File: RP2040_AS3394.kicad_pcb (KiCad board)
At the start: 4 copper layers, 51.8 x 68.3 mm, 125 parts, among them J1 Conn_01x03, J2 TYPE-C-31-M-12, J3 Conn_01x05, J4 Conn_01x09, U1 RP2040, U2 NCP1117-3.3_SOT223, U3 W25Q128JVS, U4 LM324, U5 AS3394, U6 LM324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

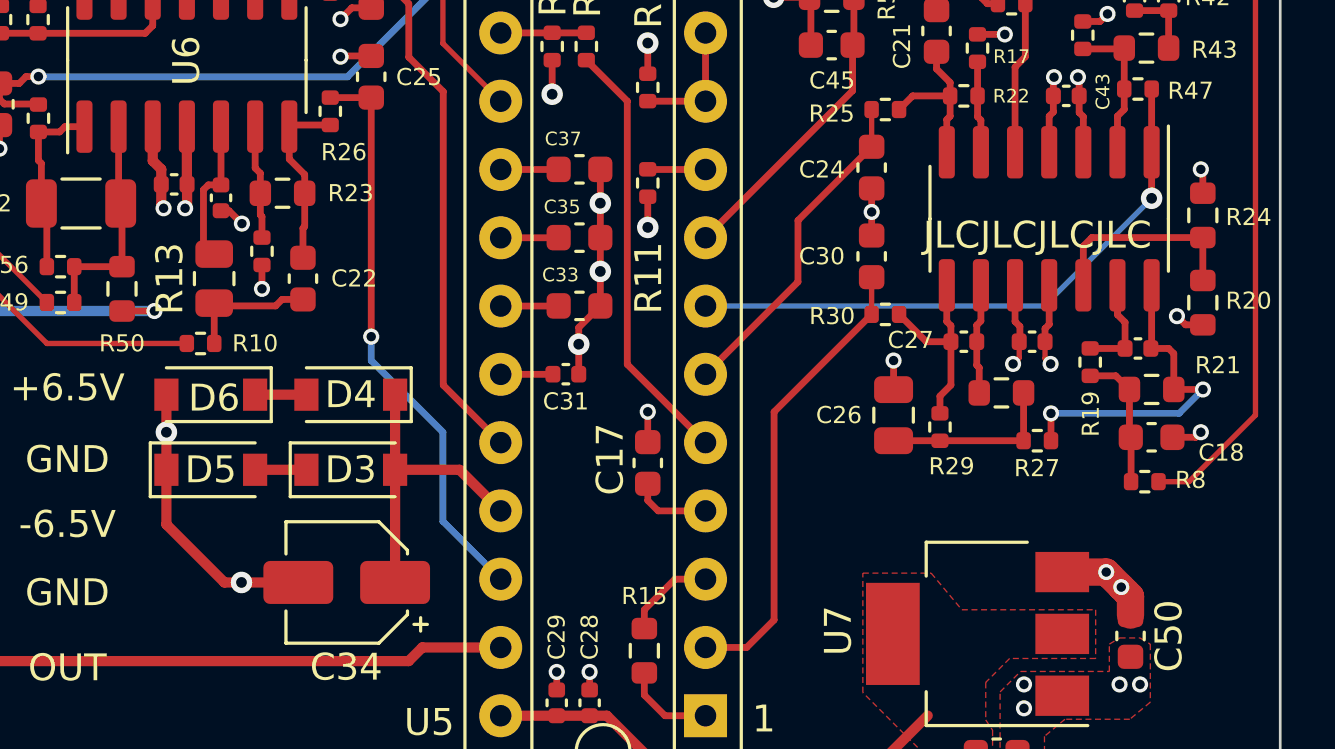
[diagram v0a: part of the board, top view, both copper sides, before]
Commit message: Updated to Kicad 7
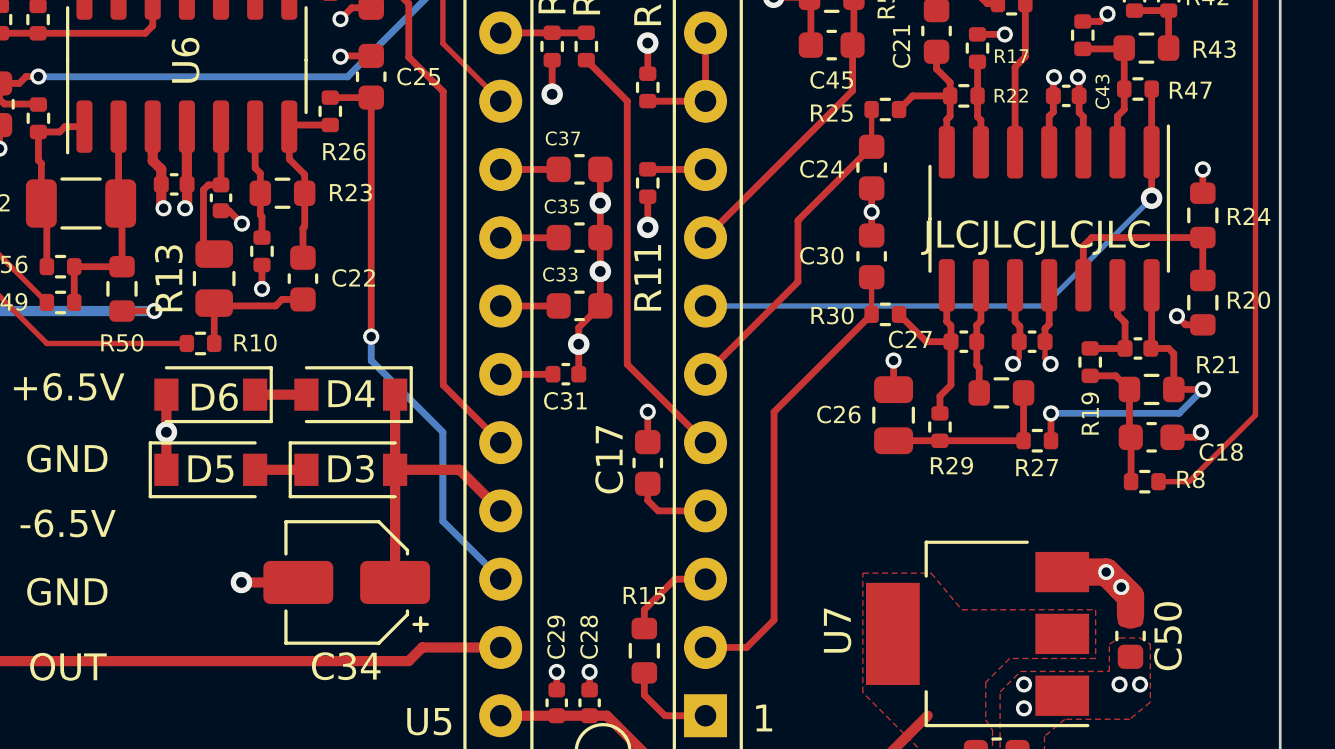
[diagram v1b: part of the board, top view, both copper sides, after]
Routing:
- net GND: track 95.2 -> 89.5 mm

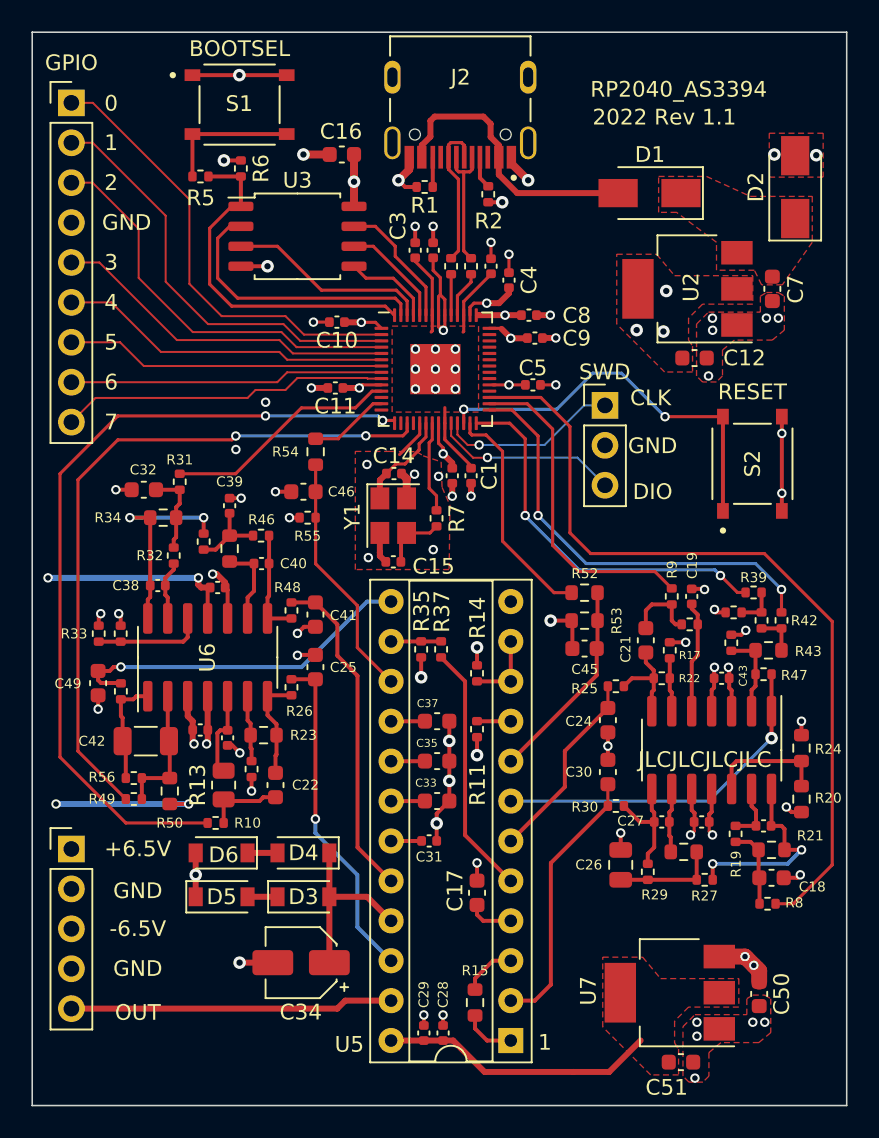
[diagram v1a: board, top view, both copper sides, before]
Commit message: Reworked op-amp bias to use 5V LDO reference instead of 6.5V vin
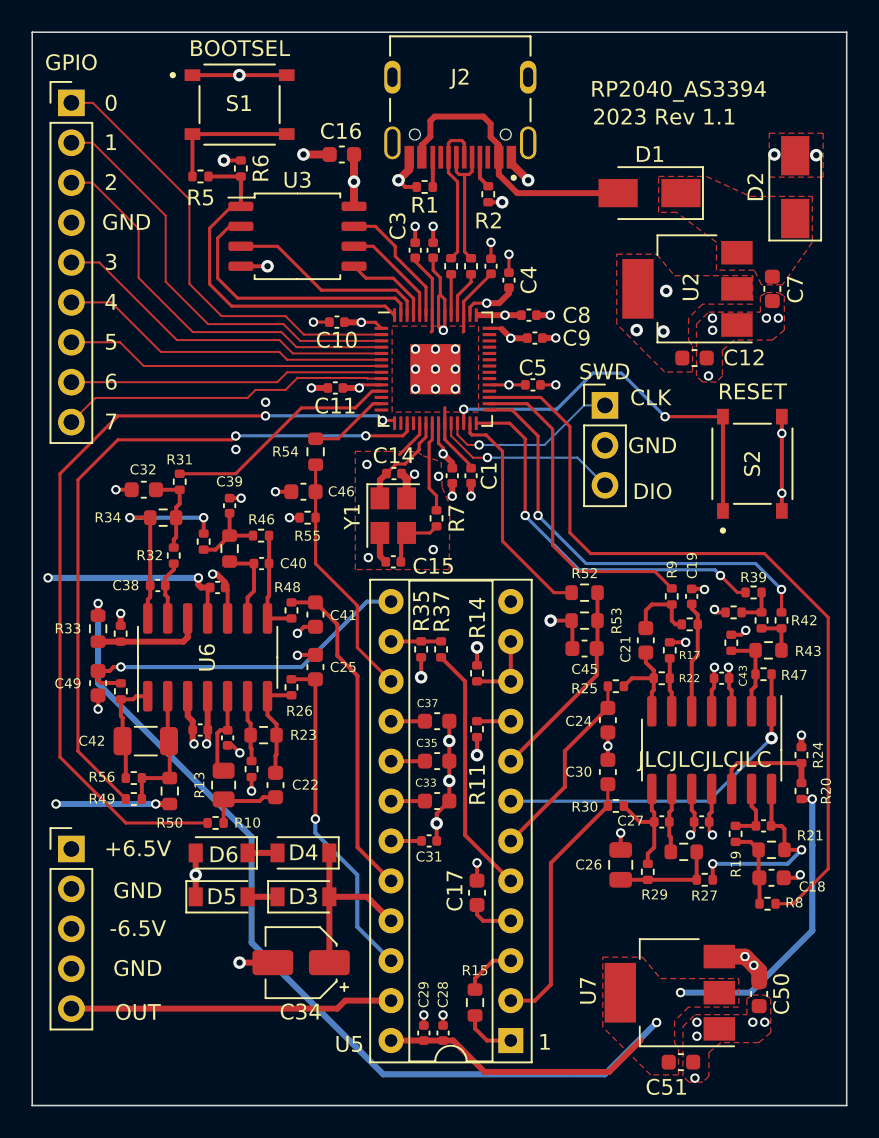
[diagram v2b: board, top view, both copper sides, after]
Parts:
- R20: value 3k -> 3k9; footprint Resistor_SMD:R_0603_1608Metric -> Resistor_SMD:R_0402_1005Metric
- R24: value 560 -> 1k; footprint Resistor_SMD:R_0603_1608Metric -> Resistor_SMD:R_0402_1005Metric
- R33: value 1k6 -> 6k2; footprint Resistor_SMD:R_0402_1005Metric -> Resistor_SMD:R_0603_1608Metric
- R36: value 300 -> 1k6
- moved R20 0.51 mm to (157.9, 131.8)
- moved R24 0.45 mm to (157.9, 129.5)
- moved R33 0.32 mm to (113.2, 121.5)
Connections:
- net /AS3394_PWM/Ext_Input2 renamed /AS3394_PWM/Pulse_Out_F/2
- R20 pad 1: VCC -> +5V
- R33 pad 1: VCC -> +5V
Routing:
- net +5V: track 17.5 -> 93.7 mm, vias 0 -> 4
- net VEE: track 49.6 -> 47.2 mm
- net VCC: track 11.5 -> 9.55 mm, vias 8 -> 6
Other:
- board text added: "2023 Rev 1.1"
- board text removed: "2022 Rev 1.1"
